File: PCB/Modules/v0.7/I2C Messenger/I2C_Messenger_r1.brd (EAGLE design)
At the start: 33.8 x 66 mm, 21 parts, among them IC1 SN65HVD31DR, IC2 PCA9517

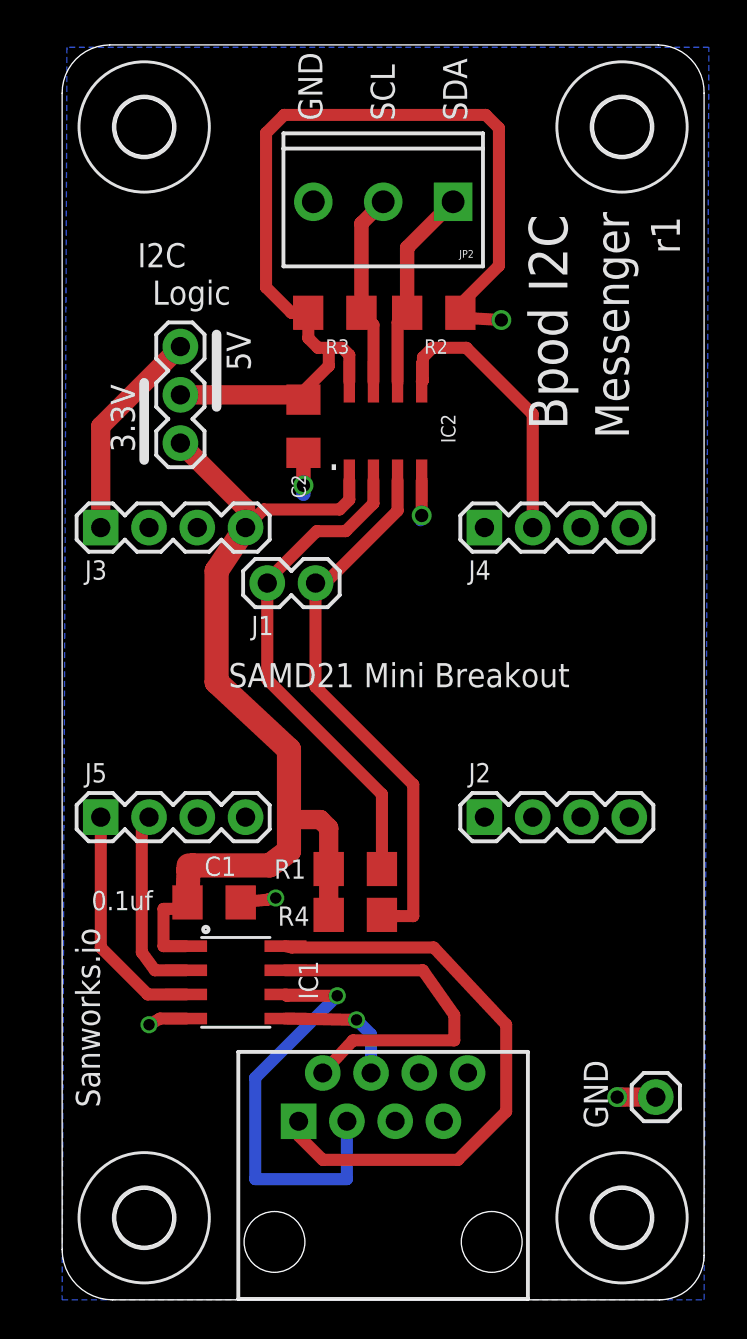
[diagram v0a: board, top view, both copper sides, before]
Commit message: - Added 8-channel analog output PCB - Updated I2C module PCB - Reorganized repository to put PCB bottom insulator designs in 1 folder -
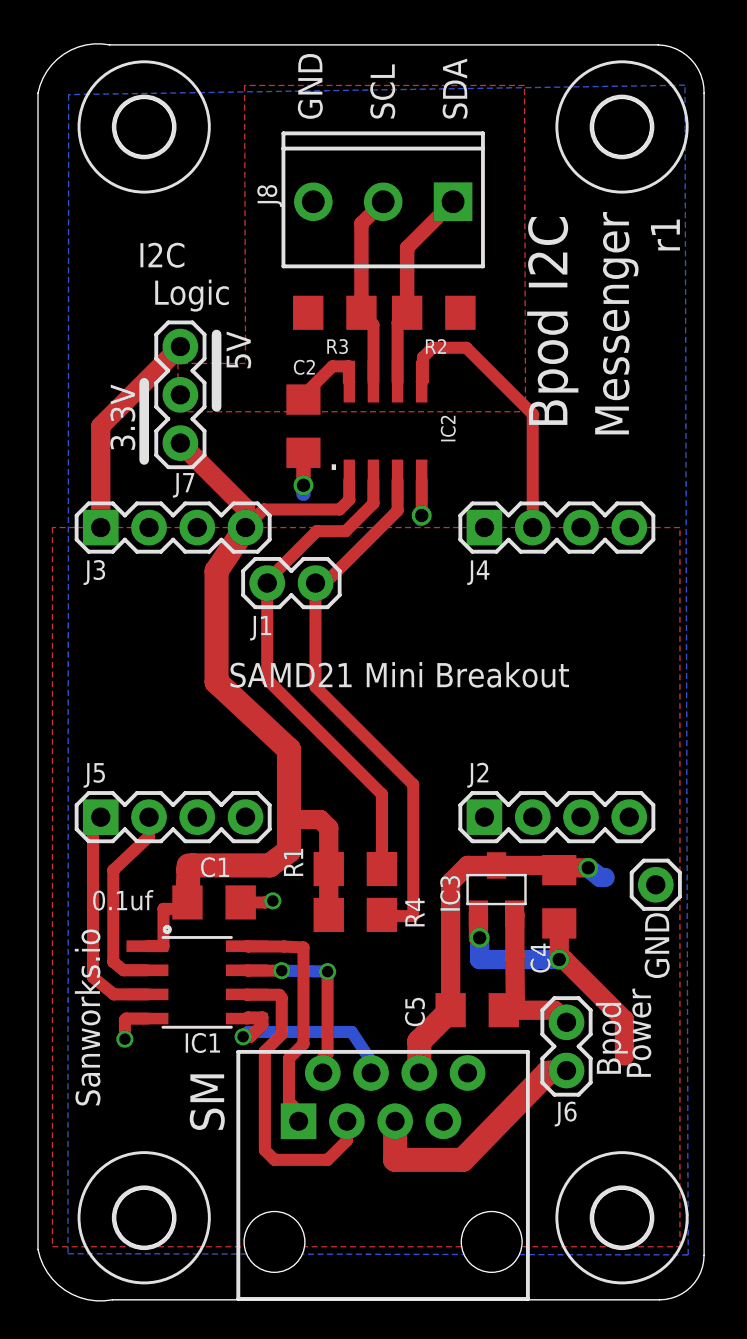
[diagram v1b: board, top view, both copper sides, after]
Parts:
- removed JP1: (no value), SparkFun-Connectors:1X03
- added C4, C5: 0.1uf, SparkFun-Capacitors:1206
- added IC3: LM3480-5.0, regulators:SOT-23-3
- added J6: (no value), SparkFun-Connectors:1X02
- added JG: (no value), SparkFun-Connectors:1X01
- J1: device SparkFun-Connectors:1X02 -> SparkFun-Connectors:1X02@1
- J7: device SparkFun-Connectors:1X01 -> SparkFun-Connectors:1X03
- moved J7 42.5 mm to (6.22, 45.1), turned to 90 degrees
- moved IC1 2.03 mm to (7.11, 16.7)
- renumbered JP2 to J8
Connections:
- new net N$1: J6.2, U$1.5
- new net N$26: C5.2, IC3.2, J6.1
- net 5V: now also C4.2, IC3.1, J7.3; no longer JP1.3
- net GND: now also C4.1, C5.1, IC3.3, JG.1, U$1.6; no longer J7.1
- net N$12: now also J7.2; no longer JP1.2
- net VCC: now also J7.1; no longer JP1.1
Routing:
- net N$12: track 51.9 -> 4.51 mm, vias 1 -> 0
- net N$7: track 31.2 -> 12.7 mm
- net GND: track 10.5 -> 27.8 mm
- net 5V: track 11.3 -> 26.5 mm, vias 0 -> 2
- net N$1: track 0.00 -> 13.0 mm
- net N$8: track 19.1 -> 9.69 mm, vias 0 -> 2
- net N$26: track 0.00 -> 9.25 mm
- net N$9: track 22.1 -> 16.3 mm, vias 1 -> 0
- net N$10: track 6.85 -> 10.8 mm
- net N$4: track 12.4 -> 11.8 mm
- added copper zone on layer 1, net 5V
- added copper zone on layer 1, net N$12
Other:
- board size 33.8 x 66 mm -> 35.1 x 66.1 mm
- board text added: "Bpod"
- board text added: "Power"
- board text added: "SM"
